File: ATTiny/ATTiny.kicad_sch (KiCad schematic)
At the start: 1 part, among them U1 ATtiny4-MA

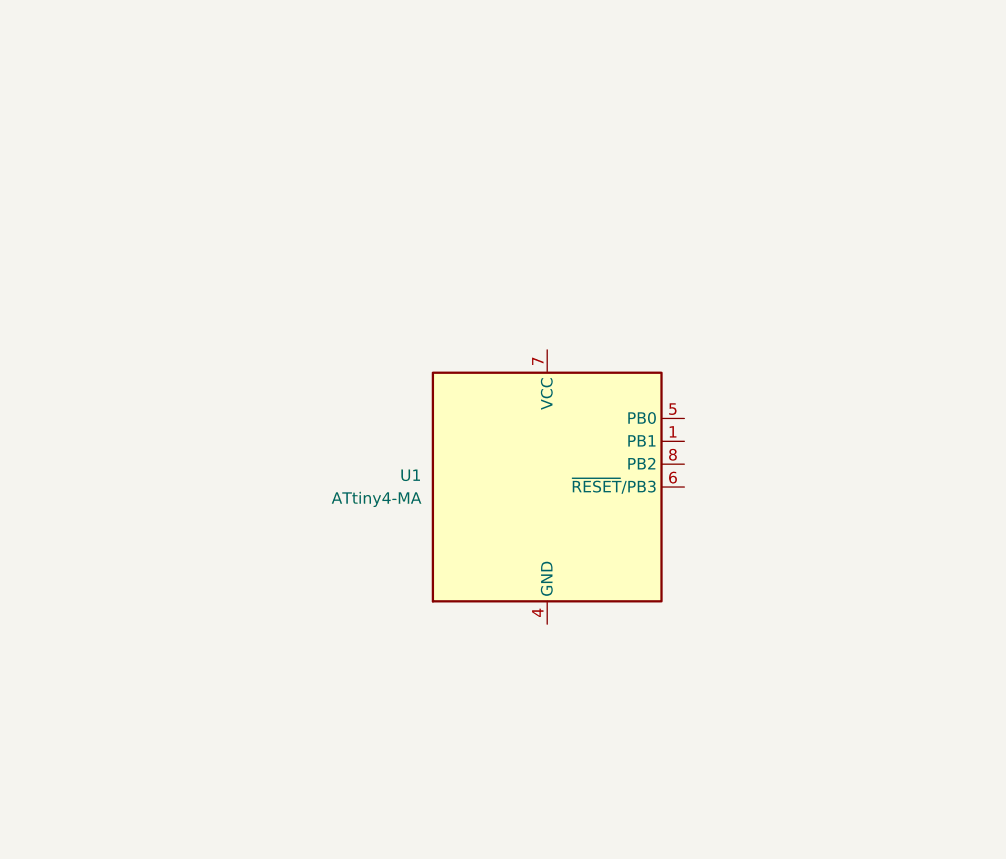
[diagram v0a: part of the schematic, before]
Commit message: ATTiny Changes
- Added components (ATTiny85-20P)and wired them in schematic
- No errors currently
- Not 100% if it would work
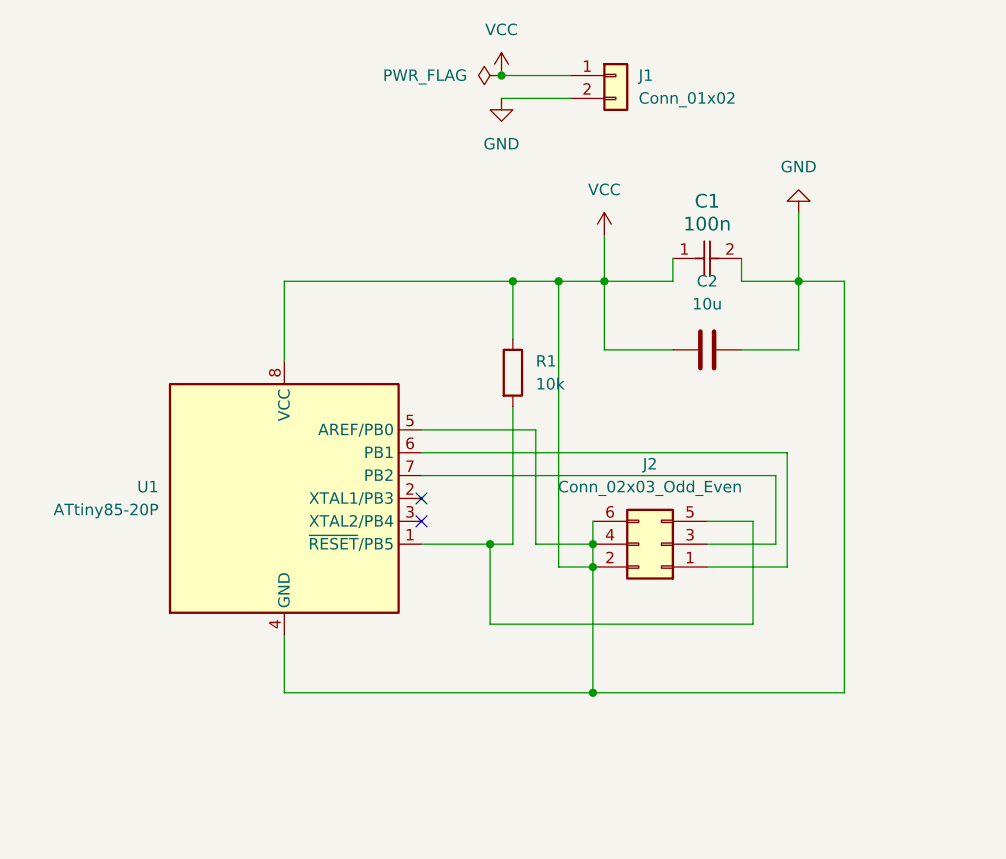
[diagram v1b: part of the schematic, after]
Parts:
- removed U1: ATtiny4-MA, Package_DFN_QFN:DFN-8-1EP_2x2mm_P0.5mm_EP0.9x1.5mm, symbol MCU_Microchip_ATtiny:ATtiny4-MA
- added C1: 100n, Capacitor_SMD:C_0603_1608Metric, symbol rsx_Capacitors:100n
- added C2: 10u, rsx_capacitors:C_0805_2012Metric, symbol rsx_Capacitors:10u
- added J1: Conn_01x02, symbol Connector_Generic:Conn_01x02
- added J2: Conn_02x03_Odd_Even, symbol Connector_Generic:Conn_02x03_Odd_Even
- added R1: 10k, rsx_resistors:R_0603_1608Metric, symbol rsx_Resistors:10k
- added U1: ATtiny85-20P, Package_DIP:DIP-8_W7.62mm, symbol MCU_Microchip_ATtiny:ATtiny85-20P
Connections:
- new net: J2.5 (Pin_5), R1.2, U1.1 (~{RESET}/PB5)
- new net: J2.1 (Pin_1), U1.6 (PB1)
- new net: J2.3 (Pin_3), U1.7 (PB2)
- new net GND: C1.1, C1.2, C2.1, C2.2, J1.1 (Pin_1), J1.2 (Pin_2), J2.2 (Pin_2), J2.4 (Pin_4), J2.6 (Pin_6), R1.1, U1.4 (GND), U1.5 (AREF/PB0), U1.8 (VCC)
- no-connect marks 0 -> 2

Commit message: hello
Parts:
- added J3: Conn_01x06_Female, rsx_headers:PinSocket_1x06_P2.54mm_Vertical, symbol rsx_header:Conn_01x06_Female
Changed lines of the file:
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@@
-	(wire
-		(pts
-			(xy 113.03 45.72) (xy 113.03 53.34)
-		)
-		(stroke
-			(width 0)
-			(type default)
-		)
-	)
 	(wire
 		(pts
@@
 			(width 0)
 			(type default)
+		)
+	)
+	(symbol
+		(lib_id "rsx_header:Conn_01x06_Female")
+		(at 133.35 77.47 0)
+		(unit 1)
+		(body_style 1)
+		(exclude_from_sim no)
+		(in_bom yes)
+		(on_board yes)
+		(in_pos_files yes)
+		(dnp no)
+		(fields_autoplaced yes)
+		(property "Reference" "J3"
+			(at 134.62 77.4699 0)
+			(show_name no)
+			(do_not_autoplace no)
+			(effects
+				(font
+					(size 1.27 1.27)
+				)
+				(justify left)
+			)
+		)
+		(property "Value" "Conn_01x06_Female"
+			(at 134.62 80.0099 0)
+			(show_name no)
+			(do_not_autoplace no)
+			(effects
+				(font
+					(size 1.27 1.27)
+				)
+				(justify left)
+			)
+		)
+		(property "Footprint" "rsx_headers:PinSocket_1x06_P2.54mm_Vertical"
+			(at 133.35 77.47 0)
+			(hide yes)
+			(show_name no)
+			(do_not_autoplace no)
+			(effects
+				(font
+					(size 1.27 1.27)
+				)
+			)
+		)
+		(property "Datasheet" ""
+			(at 133.35 77.47 0)
+			(hide yes)
+			(show_name no)
+			(do_not_autoplace no)
+			(effects
+				(font
+					(size 1.27 1.27)
+				)
+			)
+		)
+		(property "Description" "CONN HDR 6POS 0.1 TIN PCB"
+			(at 133.35 77.47 0)
+			(hide yes)
+			(show_name no)
+			(do_not_autoplace no)
+			(effects
+				(font
+					(size 1.27 1.27)
+				)
+			)
+		)
+		(property "MFR" "Sullins Connector Solutions"
+			(at 133.35 77.47 0)
+			(hide yes)
+			(show_name no)
+			(do_not_autoplace no)
+			(effects
+				(font
+					(size 1.27 1.27)
+				)
+			)
+		)
+		(property "DPN" "S7004-ND"
+			(at 133.35 77.47 0)
+			(hide yes)
+			(show_name no)
+			(do_not_autoplace no)
+			(effects
+				(font
+					(size 1.27 1.27)
+				)
+			)
+		)
+		(property "MPN" "PPTC061LFBN-RC"
+			(at 133.35 77.47 0)
+			(hide yes)
+			(show_name no)
+			(do_not_autoplace no)
+			(effects
+				(font
+					(size 1.27 1.27)
+				)
+			)
+		)
+		(pin "6"
+		)
+		(pin "2"
+		)
+		(pin "4"
+		)
+		(pin "5"
+		)
+		(pin "1"
+		)
+		(pin "3"
+		)
+		(instances
+			(project "ATTiny"
+				(path "/46ef1815-a8ed-4d38-a82f-c72395c084aa"
+					(reference "J3")
+					(unit 1)
+				)
+			)
 		)
 	)
@@
 	)
 	(symbol
+		(lib_id "power:GND")
+		(at 90.17 99.06 0)
+		(unit 1)
+		(body_style 1)
+		(exclude_from_sim no)
+		(in_bom yes)
+		(on_board yes)
+		(in_pos_files yes)
+		(dnp no)
+		(fields_autoplaced yes)
+		(property "Reference" "#PWR05"
+			(at 90.17 105.41 0)
+			(hide yes)
+			(show_name no)
+			(do_not_autoplace no)
+			(effects
+				(font
+					(size 1.27 1.27)
+				)
+			)
+		)
+		(property "Value" "GND"
+			(at 90.17 104.14 0)
+			(show_name no)
+			(do_not_autoplace no)
+			(effects
+				(font
+					(size 1.27 1.27)
+				)
+			)
+		)
+		(property "Footprint" ""
+			(at 90.17 99.06 0)
+			(hide yes)
+			(show_name no)
+			(do_not_autoplace no)
+			(effects
+				(font
+					(size 1.27 1.27)
+				)
+			)
+		)
+		(property "Datasheet" ""
+			(at 90.17 99.06 0)
+			(hide yes)
+			(show_name no)
+			(do_not_autoplace no)
+			(effects
+				(font
+					(size 1.27 1.27)
+				)
+			)
+		)
+		(property "Description" "Power symbol creates a global label with name \"GND\" , ground"
+			(at 90.17 99.06 0)
+			(hide yes)
+			(show_name no)
+			(do_not_autoplace no)
+			(effects
+				(font
+					(size 1.27 1.27)
+				)
+			)
+		)
+		(pin "1"
+		)
+		(instances
+			(project "ATTiny"
+				(path "/46ef1815-a8ed-4d38-a82f-c72395c084aa"
+					(reference "#PWR05")
+					(unit 1)
+				)
+			)
+		)
+	)
+	(symbol
 		(lib_id "Connector_Generic:Conn_01x02")
 		(at 92.71 30.48 0)
@@
 					(unit 1)
 				)
-			)
-		)
-	)
-	(symbol
-		(lib_id "power:GND")
-		(at 113.03 45.72 180)
-		(unit 1)
-		(body_style 1)
-		(exclude_from_sim no)
-		(in_bom yes)
-		(on_board yes)
-		(in_pos_files yes)
-		(dnp no)
-		(fields_autoplaced yes)
-		(property "Reference" "#PWR02"
-			(at 113.03 39.37 0)
-			(hide yes)
-			(show_name no)
-			(do_not_autoplace no)
-			(effects
-				(font
-					(size 1.27 1.27)
-				)
-			)
-		)
-		(property "Value" "GND"
-			(at 113.03 40.64 0)
-			(show_name no)
-			(do_not_autoplace no)
-			(effects
-				(font
-					(size 1.27 1.27)
-				)
-			)
-		)
-		(property "Footprint" ""
-			(at 113.03 45.72 0)
-			(hide yes)
-			(show_name no)
-			(do_not_autoplace no)
-			(effects
-				(font
-					(size 1.27 1.27)
-				)
-			)
-		)
-		(property "Datasheet" ""
-			(at 113.03 45.72 0)
-			(hide yes)
-			(show_name no)
-			(do_not_autoplace no)
-			(effects
-				(font
-					(size 1.27 1.27)
-				)
-			)
-		)
-		(property "Description" "Power symbol creates a global label with name \"GND\" , ground"
-			(at 113.03 45.72 0)
-			(hide yes)
-			(show_name no)
-			(do_not_autoplace no)
-			(effects
-				(font
-					(size 1.27 1.27)
-				)
-			)
-		)
-		(pin "1"
-		)
-		(instances
-			(project "ATTiny"
-				(path "/46ef1815-a8ed-4d38-a82f-c72395c084aa"
-					(reference "#PWR02")
-					(unit 1)
-				)

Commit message: ATTiny Schematic Done
- ATTiny Schematic Done
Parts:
- removed C1: 100n, Capacitor_SMD:C_0603_1608Metric, symbol rsx_Capacitors:100n
- removed C2: 10u, rsx_capacitors:C_0805_2012Metric, symbol rsx_Capacitors:10u
- removed J1: Conn_01x02, symbol Connector_Generic:Conn_01x02
- removed J2: Conn_02x03_Odd_Even, symbol Connector_Generic:Conn_02x03_Odd_Even
- removed J3: Conn_01x06_Female, rsx_headers:PinSocket_1x06_P2.54mm_Vertical, symbol rsx_header:Conn_01x06_Female
- removed R1: 10k, rsx_resistors:R_0603_1608Metric, symbol rsx_Resistors:10k
- removed U1: ATtiny85-20P, Package_DIP:DIP-8_W7.62mm, symbol MCU_Microchip_ATtiny:ATtiny85-20P
- added C5: 10u, rsx_capacitors:C_0805_2012Metric, symbol rsx_Capacitors:10u
- added C6: 100n, Capacitor_SMD:C_0603_1608Metric, symbol rsx_Capacitors:100n
- added J4: Conn_01x02, symbol Connector_Generic:Conn_01x02
- added J6: Conn_01x06_Female, rsx_headers:PinSocket_1x06_P2.54mm_Vertical, symbol rsx_header:Conn_01x06_Female
- added R3: 10k, rsx_resistors:R_0603_1608Metric, symbol rsx_Resistors:10k
- added U2: ATtiny85-20P, Package_DIP:DIP-8_W7.62mm, symbol MCU_Microchip_ATtiny:ATtiny85-20P
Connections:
- net GND: now also C5.2, C6.2, J4.2 (Pin_2), J6.6 (Pin_6), U2.4 (GND)
- new net: J6.5 (Pin_5), U2.1 (~{RESET}/PB5)
- new net: J6.4 (Pin_4), U2.5 (AREF/PB0)
- new net: J6.1 (Pin_1), U2.6 (PB1)
- new net: J6.3 (Pin_3), U2.7 (PB2)
- new net +5V: C5.1, C6.1, J4.1 (Pin_1), R3.2
- new net 5V: J6.2 (Pin_2), R3.1, U2.8 (VCC)

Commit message: Updates ATTiny
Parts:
- removed J4: Conn_01x02, symbol Connector_Generic:Conn_01x02
- added J1: Screw_Terminal_2x2.54, rsx_headers_screw:Wurth_691210910002, symbol rsx_header_screw:Screw_Terminal_2x2.54
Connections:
- net +5V: now also J1.1 (Pin_1)
- net GND: now also J1.2 (Pin_2)
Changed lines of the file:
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@@
+	(wire
+		(pts
+			(xy 78.74 30.48) (xy 81.28 30.48)
+		)
+		(stroke
+			(width 0)
+			(type default)
+		)
+	)
 	(wire
 		(pts
@@
 		(pts
 			(xy 78.74 36.83) (xy 78.74 33.02)
+		)
+		(stroke
+			(width 0)
+			(type default)
+		)
+	)
+	(wire
+		(pts
+			(xy 78.74 33.02) (xy 81.28 33.02)
 		)
 		(stroke
@@
 	)
 	(symbol
-		(lib_id "Connector_Generic:Conn_01x02")
-		(at 83.82 30.48 0)
-		(unit 1)
-		(body_style 1)
-		(exclude_from_sim no)
-		(in_bom yes)
-		(on_board yes)
-		(in_pos_files yes)
-		(dnp no)
-		(fields_autoplaced yes)
-		(property "Reference" "J4"
-			(at 86.36 30.4799 0)
-			(show_name no)
-			(do_not_autoplace no)
-			(effects
-				(font
-					(size 1.27 1.27)
-				)
-				(justify left)
-			)
-		)
-		(property "Value" "Conn_01x02"
-			(at 86.36 33.0199 0)
-			(show_name no)
-			(do_not_autoplace no)
-			(effects
-				(font
-					(size 1.27 1.27)
-				)
-				(justify left)
-			)
-		)
-		(property "Footprint" ""
-			(at 83.82 30.48 0)
-			(hide yes)
-			(show_name no)
-			(do_not_autoplace no)
-			(effects
-				(font
-					(size 1.27 1.27)
-				)
-			)
-		)
-		(property "Datasheet" ""
-			(at 83.82 30.48 0)
-			(hide yes)
-			(show_name no)
-			(do_not_autoplace no)
-			(effects
-				(font
-					(size 1.27 1.27)
-				)
-			)
-		)
-		(property "Description" "Generic connector, single row, 01x02, script generated (kicad-library-utils/schlib/autogen/connector/)"
-			(at 83.82 30.48 0)
-			(hide yes)
-			(show_name no)
-			(do_not_autoplace no)
-			(effects
-				(font
-					(size 1.27 1.27)
-				)
-			)
-		)
-		(pin "1"
-		)
-		(pin "2"
-		)
-		(instances
-			(project "ATTiny"
-				(path "/46ef1815-a8ed-4d38-a82f-c72395c084aa"
-					(reference "J4")
-					(unit 1)
-				)
-			)
-		)
-	)
-	(symbol
 		(lib_id "rsx_Resistors:10k")
 		(at 40.64 25.4 90)
@@
 					(unit 1)
 				)
+			)
+		)
+	)
+	(symbol
+		(lib_id "rsx_header_screw:Screw_Terminal_2x2.54")
+		(at 86.36 30.48 0)
+		(unit 1)
+		(body_style 1)
+		(exclude_from_sim no)
+		(in_bom yes)
+		(on_board yes)
+		(in_pos_files yes)
+		(dnp no)
+		(fields_autoplaced yes)
+		(property "Reference" "J1"
+			(at 88.9 31.7499 0)
+			(show_name no)
+			(do_not_autoplace no)
+			(effects
+				(font
+					(size 1.27 1.27)
+				)
+				(justify left)
+			)
+		)
+		(property "Value" "Screw_Terminal_2x2.54"
+			(at 86.36 35.56 0)
+			(hide yes)
+			(show_name no)
+			(do_not_autoplace no)
+			(effects
+				(font
+					(size 1.27 1.27)
+				)
+			)
+		)
+		(property "Footprint" "rsx_headers_screw:Wurth_691210910002"
+			(at 86.36 30.48 0)
+			(hide yes)
+			(show_name no)
+			(do_not_autoplace no)
+			(effects
+				(font
+					(size 1.27 1.27)
+				)
+			)
+		)
+		(property "Datasheet" ""
+			(at 86.36 30.48 0)
+			(hide yes)
+			(show_name no)
+			(do_not_autoplace no)
+			(effects
+				(font
+					(size 1.27 1.27)
+				)
+			)
+		)
+		(property "Description" "TERM BLOCK 2P HORIZON 2.54MM PCB"
+			(at 86.36 30.48 0)
+			(hide yes)
+			(show_name no)
+			(do_not_autoplace no)
+			(effects
+				(font
+					(size 1.27 1.27)
+				)
+			)
+		)
+		(property "MFR" "Würth Elektronik"
+			(at 86.36 30.48 0)
+			(hide yes)
+			(show_name no)
+			(do_not_autoplace no)
+			(effects
+				(font
+					(size 1.27 1.27)
+				)
+			)
+		)
+		(property "DPN" "732-691210910002-ND"
+			(at 86.36 30.48 0)
+			(hide yes)
+			(show_name no)
+			(do_not_autoplace no)
+			(effects
+				(font
+					(size 1.27 1.27)
+				)
+			)
+		)
+		(property "MPN" "691210910002"
+			(at 86.36 30.48 0)
+			(hide yes)
+			(show_name no)
+			(do_not_autoplace no)
+			(effects
+				(font
+					(size 1.27 1.27)
+				)
+			)
+		)
+		(pin "2"
+		)
+		(pin "1"
+		)
+		(instances
+			(project "ATTiny"
+				(path "/46ef1815-a8ed-4d38-a82f-c72395c084aa"
+					(reference "J1")
+					(unit 1)
+				)

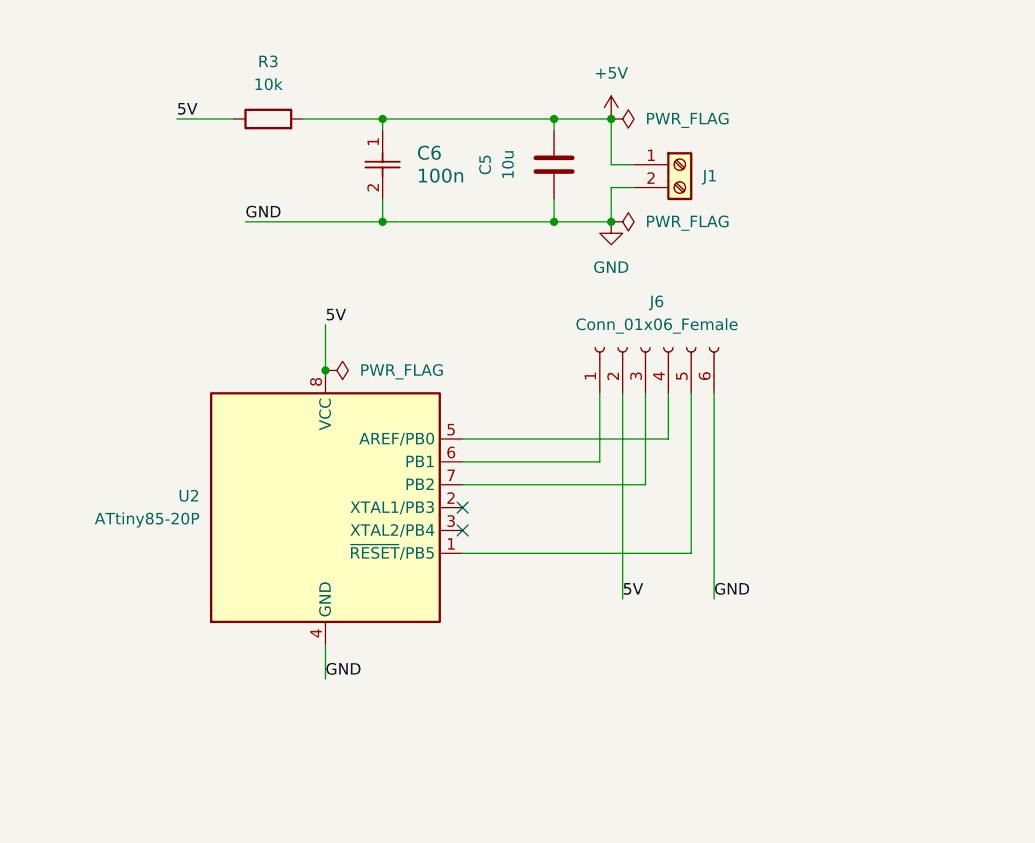
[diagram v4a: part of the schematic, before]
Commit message: Changed for ATTiny Socket & Arduino Header Stacking
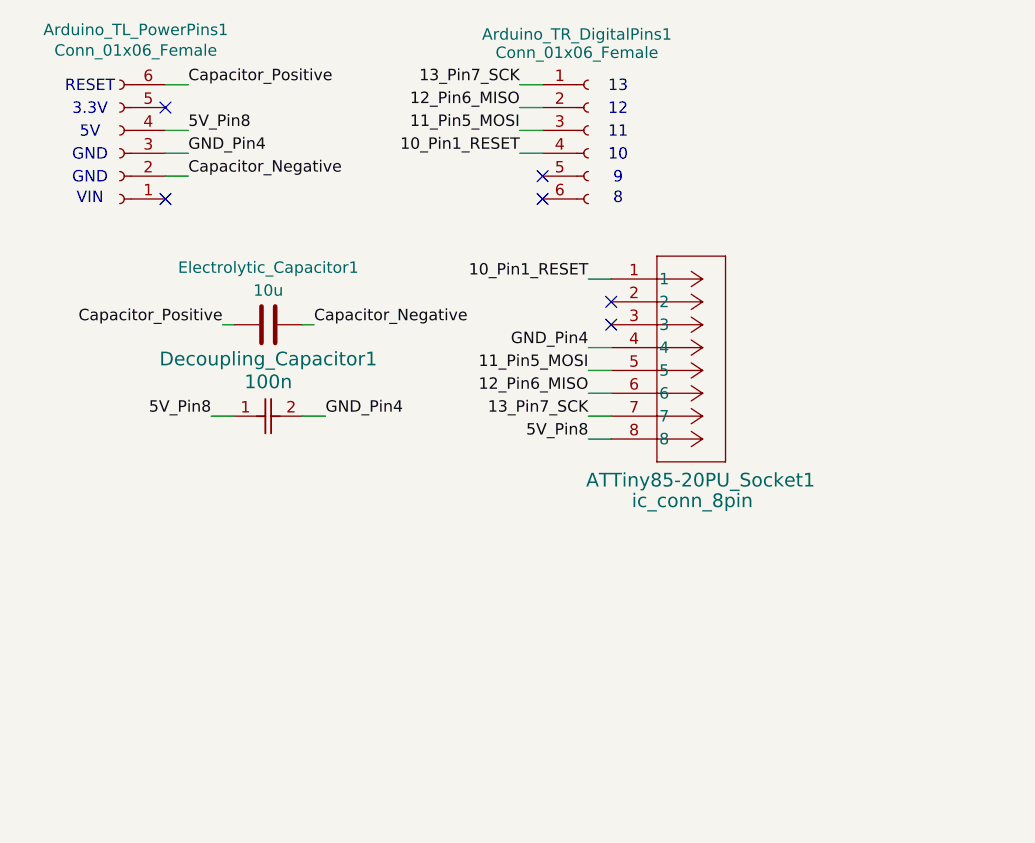
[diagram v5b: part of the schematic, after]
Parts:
- removed C5: 10u, rsx_capacitors:C_0805_2012Metric, symbol rsx_Capacitors:10u
- removed C6: 100n, Capacitor_SMD:C_0603_1608Metric, symbol rsx_Capacitors:100n
- removed J1: Screw_Terminal_2x2.54, rsx_headers_screw:Wurth_691210910002, symbol rsx_header_screw:Screw_Terminal_2x2.54
- removed J6: Conn_01x06_Female, rsx_headers:PinSocket_1x06_P2.54mm_Vertical, symbol rsx_header:Conn_01x06_Female
- removed R3: 10k, rsx_resistors:R_0603_1608Metric, symbol rsx_Resistors:10k
- removed U2: ATtiny85-20P, Package_DIP:DIP-8_W7.62mm, symbol MCU_Microchip_ATtiny:ATtiny85-20P
- added ATTiny85-20PU_Socket1: ic_conn_8pin, rsx_misc:CONN8_1-2199298-2_TEC, symbol rsx_misc:ic_conn_8pin
- added Arduino_TL_PowerPins1, Arduino_TR_DigitalPins1: Conn_01x06_Female, rsx_headers:PinSocket_1x06_P2.54mm_Vertical, symbol rsx_header:Conn_01x06_Female
- added Decoupling_Capacitor1: 100n, Capacitor_SMD:C_0603_1608Metric, symbol rsx_Capacitors:100n
- added Electrolytic_Capacitor1: 10u, rsx_capacitors:C_0805_2012Metric, symbol rsx_Capacitors:10u
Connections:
- new net 10_Pin1_RESET: ATTiny85-20PU_Socket1.1, Arduino_TR_DigitalPins1.4 (Pin_4)
- new net 11_Pin5_MOSI: ATTiny85-20PU_Socket1.5, Arduino_TR_DigitalPins1.3 (Pin_3)
- new net 12_Pin6_MISO: ATTiny85-20PU_Socket1.6, Arduino_TR_DigitalPins1.2 (Pin_2)
- new net 13_Pin7_SCK: ATTiny85-20PU_Socket1.7, Arduino_TR_DigitalPins1.1 (Pin_1)
- new net 5V_Pin8: ATTiny85-20PU_Socket1.8, Arduino_TL_PowerPins1.4 (Pin_4), Decoupling_Capacitor1.1
- new net Capacitor_Negative: Arduino_TL_PowerPins1.2 (Pin_2), Electrolytic_Capacitor1.1
- new net Capacitor_Positive: Arduino_TL_PowerPins1.6 (Pin_6), Electrolytic_Capacitor1.2
- new net GND_Pin4: ATTiny85-20PU_Socket1.4, Arduino_TL_PowerPins1.3 (Pin_3), Decoupling_Capacitor1.2
- no-connect marks 2 -> 6
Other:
- note added: "10"
- note added: "11"
- note added: "12"
- note added: "13"
- note added: "3.3V"
- note added: "5V"
- note added: "8"
- note added: "9"
- note added: "GND"
- note added: "RESET"
- note added: "VIN"

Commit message: Adj ATTiny
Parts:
- removed Electrolytic_Capacitor1: 10u, rsx_capacitors:C_0805_2012Metric, symbol rsx_Capacitors:10u
- added Electrolytic_Capacitor_Arduino1: 10u, rsx_capacitors:C_0805_2012Metric, symbol rsx_Capacitors:10u
- added R1: 10k, rsx_resistors:R_0603_1608Metric, symbol rsx_Resistors:10k
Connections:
- net Capacitor_Negative: now also Electrolytic_Capacitor_Arduino1.1
- net Capacitor_Positive: now also Electrolytic_Capacitor_Arduino1.2
- net 10_Pin1_RESET renamed RESET
- net 11_Pin5_MOSI renamed MOSI
- net 12_Pin6_MISO renamed MISO
- net 13_Pin7_SCK: no longer names the net of Arduino_TR_DigitalPins1.1 (Pin_1)
- net 13_Pin7_SCK: now also R1.2; no longer ATTiny85-20PU_Socket1.7
- net 5V_Pin8 renamed 5V
- net GND_Pin4 renamed GND
- new net SCK: ATTiny85-20PU_Socket1.7, R1.1

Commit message: ATTiny Adjust
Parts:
- removed Arduino_TL_PowerPins1, Arduino_TR_DigitalPins1: Conn_01x06_Female, rsx_headers:PinSocket_1x06_P2.54mm_Vertical, symbol rsx_header:Conn_01x06_Female
- removed R1: 10k, rsx_resistors:R_0603_1608Metric, symbol rsx_Resistors:10k
- added Arduino_BL1, Arduino_TR_2: header_1x6_arduino, Connector_PinHeader_2.54mm:PinHeader_1x06_P2.54mm_Vertical, symbol rsx_header:header_1x6_arduino
- added Arduino_BR1, Arduino_TL1: header_1x8_arduino, Connector_PinHeader_2.54mm:PinHeader_1x08_P2.54mm_Vertical, symbol rsx_header:header_1x8_arduino
- added Arduino_TR_1: header_1x4_arduino, Connector_PinHeader_2.54mm:PinHeader_1x04_P2.54mm_Vertical, symbol rsx_header:header_1x4_arduino
- added R2: 10k, rsx_resistors:R_0603_1608Metric, symbol rsx_Resistors:10k
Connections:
- net 5V: now also Arduino_TL1.4
- net Capacitor_Negative: now also Arduino_TL1.2
- net Capacitor_Positive: now also Arduino_TL1.6
- net GND: now also Arduino_TL1.3
- net MISO: now also Arduino_TR_2.2
- net MOSI: now also Arduino_TR_2.3
- net RESET: now also Arduino_TR_2.4
- net SCK: now also R2.1
- new net: Arduino_TR_2.1, R2.2
- no-connect marks 6 -> 26
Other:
- note added: "ANALOG PINS"
- note added: "DIGITAL PWM"
- note added: "IOREF"
- note added: "NC"
- note added: "~10"
- note added: "~11"
- note added: "~9"
- note removed: "10"
- note removed: "11"
- note removed: "9"
